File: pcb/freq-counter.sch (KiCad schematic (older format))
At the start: 62 parts, among them J1 RPM on board, J10 Power_T1, J11 Hz/RPM_Terminal1, J12 Hz/RPM_Terminal0, J2 BNC, J3 RPM to Board, J4 Jack-DC, J5 Segments-Terminal0, J6 Digits-Terminal0, J7 Segments-Terminal1, J8 Digits-Terminal1, J9 Power_Terminal1, Q1 CSC388A, Q2 CSC388A, Q3 2SA1015, Q4 2SC1815, Q5 2SC1815, SW1 on/off, SW2 count up, SW3 toggle, SW4 SW_SIGNAL, U1 SN74HC02N, U2 ATTINY4313-PU(freq-counter), U3 EE-SX460, Y1 10MHz

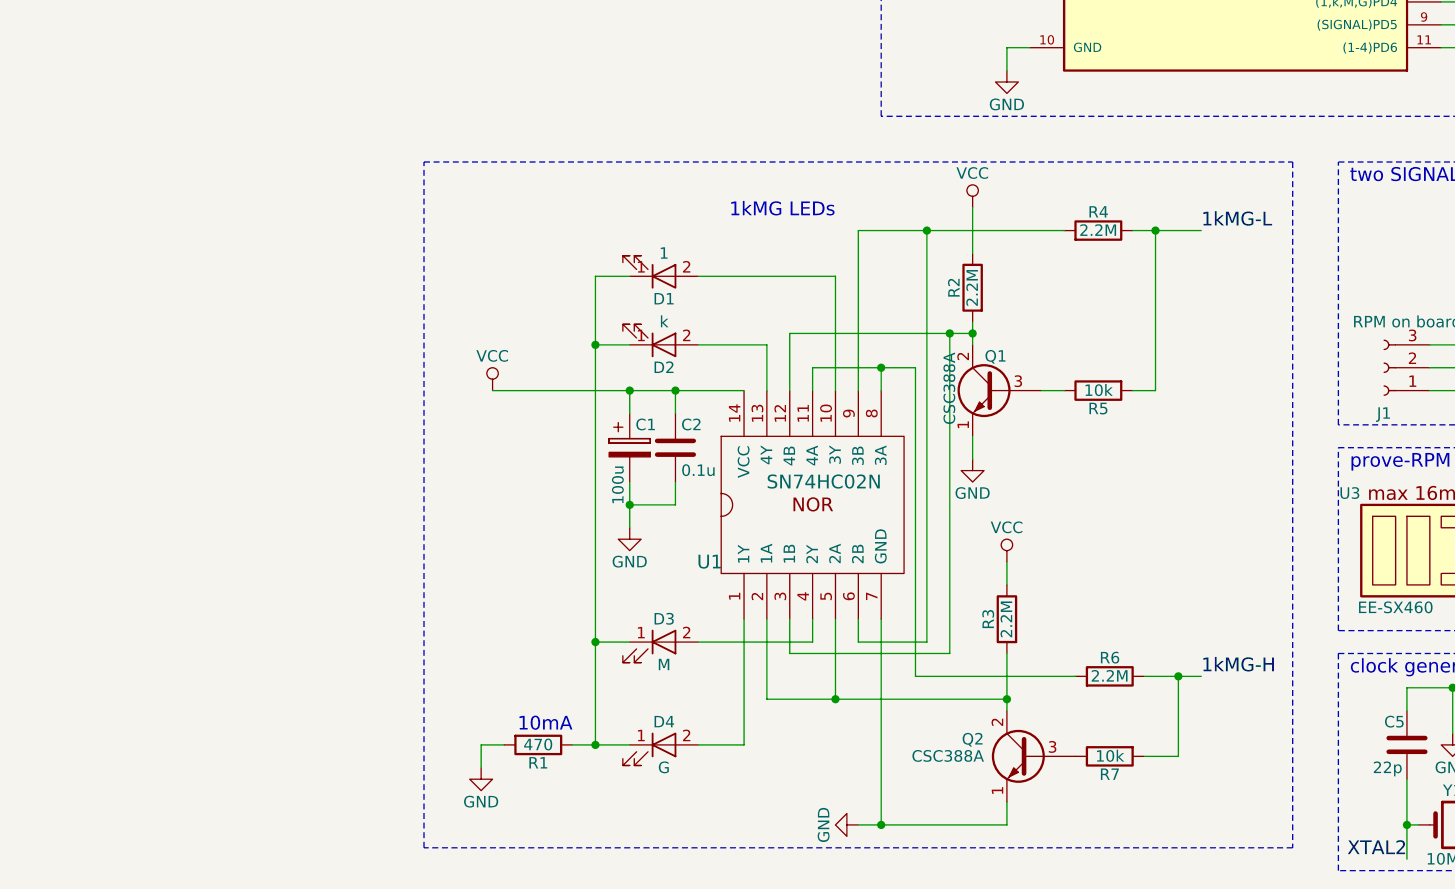
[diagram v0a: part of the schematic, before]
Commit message: 1kMG-LED 部のTerminal化が完了。
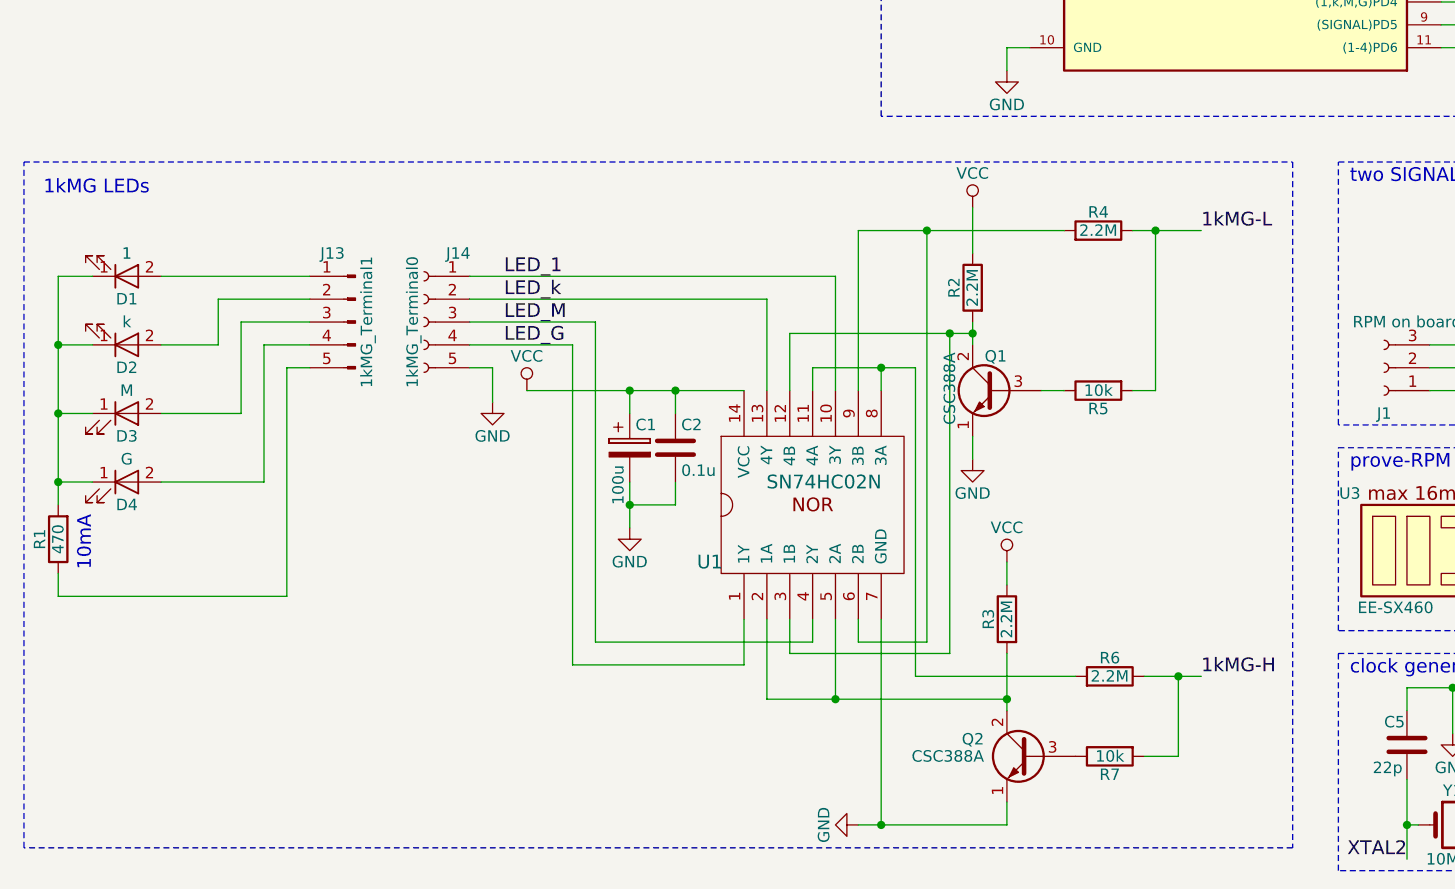
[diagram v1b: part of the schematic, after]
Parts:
- added J13: 1kMG_Terminal1, Connector_PinHeader_2.54mm:PinHeader_1x05_P2.54mm_Vertical, symbol Conn_01x05_Male
- added J14: 1kMG_Terminal0, Connector_PinSocket_2.54mm:PinSocket_1x05_P2.54mm_Vertical, symbol Conn_01x05_Female
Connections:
- net GND: now also J14.5 (Pin_5); no longer R1.2
- net at D1.1 (K), D2.1 (K), D3.1 (K)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: now also R1.2; no longer R1.1
- net at D4.2 (A): now also J13.4 (Pin_4); no longer U1.1 (1Y)
- net at D3.2 (A): now also J13.3 (Pin_3); no longer U1.4 (2Y)
- net at D2.2 (A): now also J13.2 (Pin_2); no longer U1.13 (4Y)
- net at D1.2 (A): now also J13.1 (Pin_1); no longer U1.10 (3Y)
- new net: J13.5 (Pin_5), R1.1
- new net LED_1: J14.1 (Pin_1), U1.10 (3Y)
- new net LED_G: J14.4 (Pin_4), U1.1 (1Y)
- new net LED_M: J14.3 (Pin_3), U1.4 (2Y)
- new net LED_k: J14.2 (Pin_2), U1.13 (4Y)
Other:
- moved on the sheet: D1, D2, D3, D4, R1
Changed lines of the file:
@@
 L LED D4
 U 1 1 5A031894
-P 1600 6050
-F 0 "D4" H 1600 6150 50  0000 C CNN
-F 1 "G" H 1600 5950 50  0000 C CNN
-F 2 "LEDs:LED_D5.0mm" H 1600 6050 50  0001 C CNN
-F 3 "" H 1600 6050 50  0001 C CNN
-	1    1600 6050
+P -750 4900
+F 0 "D4" H -750 4800 50  0000 C CNN
+F 1 "G" H -750 5000 50  0000 C CNN
+F 2 "LEDs:LED_D5.0mm" H -750 4900 50  0001 C CNN
+F 3 "" H -750 4900 50  0001 C CNN
+	1    -750 4900
 	1    0    0    -1
 $EndComp
@@
 L LED D3
 U 1 1 5A0318C9
-P 1600 5600
-F 0 "D3" H 1600 5700 50  0000 C CNN
-F 1 "M" H 1600 5500 50  0000 C CNN
-F 2 "LEDs:LED_D5.0mm" H 1600 5600 50  0001 C CNN
-F 3 "" H 1600 5600 50  0001 C CNN
-	1    1600 5600
+P -750 4600
+F 0 "D3" H -750 4500 50  0000 C CNN
+F 1 "M" H -750 4700 50  0000 C CNN
+F 2 "LEDs:LED_D5.0mm" H -750 4600 50  0001 C CNN
+F 3 "" H -750 4600 50  0001 C CNN
+	1    -750 4600
 	1    0    0    -1
 $EndComp
@@
 L LED D2
 U 1 1 5A0318F4
-P 1600 4300
-F 0 "D2" H 1600 4400 50  0000 C CNN
-F 1 "k" H 1600 4200 50  0000 C CNN
-F 2 "LEDs:LED_D5.0mm" H 1600 4300 50  0001 C CNN
-F 3 "" H 1600 4300 50  0001 C CNN
-	1    1600 4300
+P -750 4300
+F 0 "D2" H -750 4400 50  0000 C CNN
+F 1 "k" H -750 4200 50  0000 C CNN
+F 2 "LEDs:LED_D5.0mm" H -750 4300 50  0001 C CNN
+F 3 "" H -750 4300 50  0001 C CNN
+	1    -750 4300
 	1    0    0    1
 $EndComp
@@
 L LED D1
 U 1 1 5A05AA03
-P 1600 4000
-F 0 "D1" H 1600 4100 50  0000 C CNN
-F 1 "1" H 1600 3900 50  0000 C CNN
-F 2 "LEDs:LED_D5.0mm" H 1600 4000 50  0001 C CNN
-F 3 "" H 1600 4000 50  0001 C CNN
-	1    1600 4000
+P -750 4000
+F 0 "D1" H -750 4100 50  0000 C CNN
+F 1 "1" H -750 3900 50  0000 C CNN
+F 2 "LEDs:LED_D5.0mm" H -750 4000 50  0001 C CNN
+F 3 "" H -750 4000 50  0001 C CNN
+	1    -750 4000
 	1    0    0    1
 $EndComp
@@
 L R R1
 U 1 1 5A06506A
-P 1050 6050
-F 0 "R1" V 1130 6050 50  0000 C CNN
-F 1 "470" V 1050 6050 50  0000 C CNN
-F 2 "Resistors_THT:R_Axial_DIN0207_L6.3mm_D2.5mm_P7.62mm_Horizontal" V 980 6050 50  0001 C CNN
-F 3 "" H 1050 6050 50  0001 C CNN
-	1    1050 6050
-	0    1    1    0
+P -1050 5150
+F 0 "R1" V -970 5150 50  0000 C CNN
+F 1 "470" V -1050 5150 50  0000 C CNN
+F 2 "Resistors_THT:R_Axial_DIN0207_L6.3mm_D2.5mm_P7.62mm_Horizontal" V -1120 5150 50  0001 C CNN
+F 3 "" H -1050 5150 50  0001 C CNN
+	1    -1050 5150
+	-1   0    0    1
 $EndComp
 $Comp
@@
 Text Notes 7800 3650 0    60   ~ 0
 Hz/RPM LEDs
-Text Notes 2350 3750 2    60   ~ 0
+Text Notes -650 3650 2    60   ~ 0
 1kMG LEDs
 Text Label 10650 3950 0    60   ~ 0
@@
 Text Notes 10000 4650 0    60   ~ 0
 10mA
-Text Notes 1200 6000 2    60   ~ 0
+Text Notes -900 5050 3    60   ~ 0
 10mA
 $Sheet
@@
 L VCC #PWR013
 U 1 1 5A1EAB1C
-P 850 4500
-F 0 "#PWR013" H 850 4350 50  0001 C CNN
-F 1 "VCC" H 850 4650 50  0000 C CNN
-F 2 "" H 850 4500 50  0001 C CNN
-F 3 "" H 850 4500 50  0001 C CNN
-	1    850  4500
+P 1000 4500
+F 0 "#PWR013" H 1000 4350 50  0001 C CNN
+F 1 "VCC" H 1000 4650 50  0000 C CNN
+F 2 "" H 1000 4500 50  0001 C CNN
+F 3 "" H 1000 4500 50  0001 C CNN
+	1    1000 4500
 	1    0    0    -1
 $EndComp
@@
 L GND #PWR016
 U 1 1 5A1ED93F
-P 800 6150
-F 0 "#PWR016" H 800 5900 50  0001 C CNN
-F 1 "GND" H 800 6000 50  0000 C CNN
-F 2 "" H 800 6150 50  0001 C CNN
-F 3 "" H 800 6150 50  0001 C CNN
-	1    800  6150
+P 850 4550
+F 0 "#PWR016" H 850 4300 50  0001 C CNN
+F 1 "GND" H 850 4400 50  0000 C CNN
+F 2 "" H 850 4550 50  0001 C CNN
+F 3 "" H 850 4550 50  0001 C CNN
+	1    850  4550
 	1    0    0    -1
 $EndComp
@@
 $EndComp
 Wire Wire Line
-	2050 4300 1750 4300
-Wire Wire Line
-	2050 4500 2050 4300
-Wire Wire Line
-	1750 4000 2350 4000
+	-350 4300 -600 4300
+Wire Wire Line
+	2050 4100 2050 4500
+Wire Wire Line
+	-600 4000 50   4000
 Wire Wire Line
 	2350 4000 2350 4500
 Wire Wire Line
-	850  4500 1950 4500
+	1000 4500 1950 4500
 Wire Wire Line
 	2950 3900 2950 3700
@@
 	4350 3500 4350 6500
 Wire Notes Line
-	550  3500 4350 3500
-Wire Notes Line
-	550  6500 550  3500
-Wire Notes Line
-	4350 6500 550  6500
+	-1200 3500 4350 3500
+Wire Notes Line
+	-1200 6500 -1200 3500
+Wire Notes Line
+	4350 6500 -1200 6500
 Wire Notes Line
 	9150 2300 9150 750
@@
 	3850 5750 3850 6100
 Wire Wire Line
-	1200 6050 1450 6050
-Wire Wire Line
-	1300 5600 1450 5600
+	-1050 4000 -1050 5000
+Wire Wire Line
+	-1050 4900 -900 4900
+Wire Wire Line
+	-1050 4600 -900 4600
 Wire Wire Line
 	3400 6100 3400 6100
@@
 	2250 5500 2250 5600
 Wire Wire Line
-	2250 5600 1750 5600
-Wire Wire Line
-	1950 5500 1950 6050
-Wire Wire Line
-	1950 6050 1750 6050
+	-250 4600 -600 4600
+Wire Wire Line
+	1950 5500 1950 5700
+Wire Wire Line
+	-600 4900 -150 4900
 Wire Wire Line
 	2450 5500 2450 5600
@@
 Connection ~ 2350 5850
 Wire Wire Line
-	800  6050 900  6050
-Wire Wire Line
-	1300 4300 1450 4300
-Wire Wire Line
-	1300 4000 1450 4000
+	-1050 5400 -1050 5300
+Wire Wire Line
+	-1050 4300 -900 4300
+Wire Wire Line
+	-1050 4000 -900 4000
 Wire Wire Line
 	1450 4600 1450 4500
@@
 Wire Wire Line
 	6550 5300 6650 5300
-Wire Wire Line
-	1300 4000 1300 6050
-Connection ~ 1300 6050
-Connection ~ 1300 5600
-Connection ~ 1300 4300
+Connection ~ -1050 4900
+Connection ~ -1050 4600
+Connection ~ -1050 4300
 Wire Wire Line
 	2800 1100 3200 1100
@@
 	2450 6400 3100 6400
 Connection ~ 2550 6400
-Wire Wire Line
-	800  6150 800  6050
 Wire Wire Line
 	7900 6150 7900 6050
@@
 Wire Wire Line
 	9600 5550 8900 5550
+$Comp
+L Conn_01x05_Female J14
+U 1 1 5A1F7FC1
+P 550 4200
+F 0 "J14" H 400 4500 50  0000 C CNN
+F 1 "1kMG_Terminal0" V 600 4200 50  0000 C CNN
+F 2 "Connector_PinSocket_2.54mm:PinSocket_1x05_P2.54mm_Vertical" H 550 4200 50  0001 C CNN
+F 3 "" H 550 4200 50  0001 C CNN
+	1    550  4200
+	-1   0    0    -1
+$EndComp
+$Comp
+L Conn_01x05_Male J13
+U 1 1 5A1F810E
+P 250 4200
+F 0 "J13" H 350 4500 50  0000 C CNN
+F 1 "1kMG_Terminal1" V 200 4200 50  0000 C CNN
+F 2 "Connector_PinHeader_2.54mm:PinHeader_1x05_P2.54mm_Vertical" H 250 4200 50  0001 C CNN
+F 3 "" H 250 4200 50  0001 C CNN
+	1    250  4200
+	-1   0    0    -1
+$EndComp
+Wire Wire Line
+	-350 4300 -350 4100
+Wire Wire Line
+	-350 4100 50   4100
+Wire Wire Line
+	-250 4600 -250 4200
+Wire Wire Line
+	-250 4200 50   4200
+Wire Wire Line
+	-150 4900 -150 4300
+Wire Wire Line
+	-150 4300 50   4300
+Wire Wire Line
+	-50  5400 -1050 5400
+Wire Wire Line
+	750  4000 2350 4000
+Wire Wire Line
+	750  4100 2050 4100
+Wire Wire Line
+	750  4300 1200 4300
+Wire Wire Line
+	1200 4300 1200 5700
+Wire Wire Line
+	1200 5700 1950 5700
+Wire Wire Line
+	750  4200 1300 4200
+Wire Wire Line
+	1300 4200 1300 5600
+Wire Wire Line
+	1300 5600 2250 5600
+Wire Wire Line
+	750  4400 850  4400
+Wire Wire Line
+	850  4400 850  4550
+Wire Wire Line
+	-50  5400 -50  4400
+Wire Wire Line
+	-50  4400 50   4400
+Text Label 900  4000 0    60   ~ 0
+LED_1
+Text Label 900  4100 0    60   ~ 0
+LED_k
+Text Label 900  4200 0    60   ~ 0
+LED_M
+Text Label 900  4300 0    60   ~ 0
+LED_G
 $EndSCHEMATC

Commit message: LED に関してのCvPcbをやり直した。
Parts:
- D1, D2, D3, D4, D5, D6: footprint LEDs:LED_D5.0mm -> LED_THT:LED_D5.0mm
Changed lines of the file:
@@
 F 0 "D4" H -750 4800 50  0000 C CNN
 F 1 "G" H -750 5000 50  0000 C CNN
-F 2 "LEDs:LED_D5.0mm" H -750 4900 50  0001 C CNN
+F 2 "LED_THT:LED_D5.0mm" H -750 4900 50  0001 C CNN
 F 3 "" H -750 4900 50  0001 C CNN
 	1    -750 4900
@@
 F 0 "D3" H -750 4500 50  0000 C CNN
 F 1 "M" H -750 4700 50  0000 C CNN
-F 2 "LEDs:LED_D5.0mm" H -750 4600 50  0001 C CNN
+F 2 "LED_THT:LED_D5.0mm" H -750 4600 50  0001 C CNN
 F 3 "" H -750 4600 50  0001 C CNN
 	1    -750 4600
@@
 F 0 "D2" H -750 4400 50  0000 C CNN
 F 1 "k" H -750 4200 50  0000 C CNN
-F 2 "LEDs:LED_D5.0mm" H -750 4300 50  0001 C CNN
+F 2 "LED_THT:LED_D5.0mm" H -750 4300 50  0001 C CNN
 F 3 "" H -750 4300 50  0001 C CNN
 	1    -750 4300
@@
 F 0 "D1" H -750 4100 50  0000 C CNN
 F 1 "1" H -750 3900 50  0000 C CNN
-F 2 "LEDs:LED_D5.0mm" H -750 4000 50  0001 C CNN
+F 2 "LED_THT:LED_D5.0mm" H -750 4000 50  0001 C CNN
 F 3 "" H -750 4000 50  0001 C CNN
 	1    -750 4000
@@
 F 0 "D6" H 10300 4350 50  0000 C CNN
 F 1 "Hz" H 10250 4550 50  0000 C CNN
-F 2 "LEDs:LED_D5.0mm" H 10300 4450 50  0001 C CNN
+F 2 "LED_THT:LED_D5.0mm" H 10300 4450 50  0001 C CNN
 F 3 "" H 10300 4450 50  0001 C CNN
 	1    10300 4450
@@
 F 0 "D5" H 9900 4350 50  0000 C CNN
 F 1 "RPM" H 9950 4550 50  0000 C CNN
-F 2 "LEDs:LED_D5.0mm" H 9900 4450 50  0001 C CNN
+F 2 "LED_THT:LED_D5.0mm" H 9900 4450 50  0001 C CNN
 F 3 "" H 9900 4450 50  0001 C CNN
 	1    9900 4450

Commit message: transistor には，CvPcbをやり直した。
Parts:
- Q1, Q2, Q3, Q4, Q5: footprint TO_SOT_Packages_THT:TO-92_Inline_Wide -> Package_TO_SOT_THT:TO-92_Inline_Wide
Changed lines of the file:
@@
 F 0 "Q2" H 3400 6175 50  0000 L CNN
 F 1 "CSC388A" H 3400 6100 50  0000 L CNN
-F 2 "TO_SOT_Packages_THT:TO-92_Inline_Wide" H 3400 6025 50  0001 L CIN
+F 2 "Package_TO_SOT_THT:TO-92_Inline_Wide" H 3400 6025 50  0001 L CIN
 F 3 "" H 3200 6100 50  0001 L CNN
 	1    3200 6100
@@
 F 0 "Q1" H 3000 4650 50  0000 L CNN
 F 1 "CSC388A" V 3250 4350 50  0000 L CNN
-F 2 "TO_SOT_Packages_THT:TO-92_Inline_Wide" H 3250 4425 50  0001 L CIN
+F 2 "Package_TO_SOT_THT:TO-92_Inline_Wide" H 3250 4425 50  0001 L CIN
 F 3 "" H 3050 4500 50  0001 L CNN
 	1    3050 4500
@@
 F 0 "Q5" H 10000 5250 50  0000 L CNN
 F 1 "2SC1815" V 10350 5050 50  0000 L CNN
-F 2 "TO_SOT_Packages_THT:TO-92_Inline_Wide" H 10350 5125 50  0001 L CIN
+F 2 "Package_TO_SOT_THT:TO-92_Inline_Wide" H 10350 5125 50  0001 L CIN
 F 3 "" H 10150 5200 50  0001 L CNN
 	1    10150 5200
@@
 F 0 "Q4" H 8800 5300 50  0000 L CNN
 F 1 "2SC1815" V 9100 5000 50  0000 L CNN
-F 2 "TO_SOT_Packages_THT:TO-92_Inline_Wide" H 9100 5075 50  0001 L CIN
+F 2 "Package_TO_SOT_THT:TO-92_Inline_Wide" H 9100 5075 50  0001 L CIN
 F 3 "" H 8900 5150 50  0001 L CNN
 	1    8900 5150
@@
 F 0 "Q3" V 8950 4150 50  0000 L CNN
 F 1 "2SA1015" V 9050 4100 50  0000 L CNN
-F 2 "TO_SOT_Packages_THT:TO-92_Inline_Wide" H 9000 3975 50  0001 L CIN
+F 2 "Package_TO_SOT_THT:TO-92_Inline_Wide" H 9000 3975 50  0001 L CIN
 F 3 "" H 8800 4050 50  0001 L CNN
 	1    8800 4050
